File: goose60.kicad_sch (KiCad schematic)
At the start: 32 parts, among them SW1 SW_Push, SW2 SW_Push, U1 STM32F103CBTx, X1 Crystal_GND24

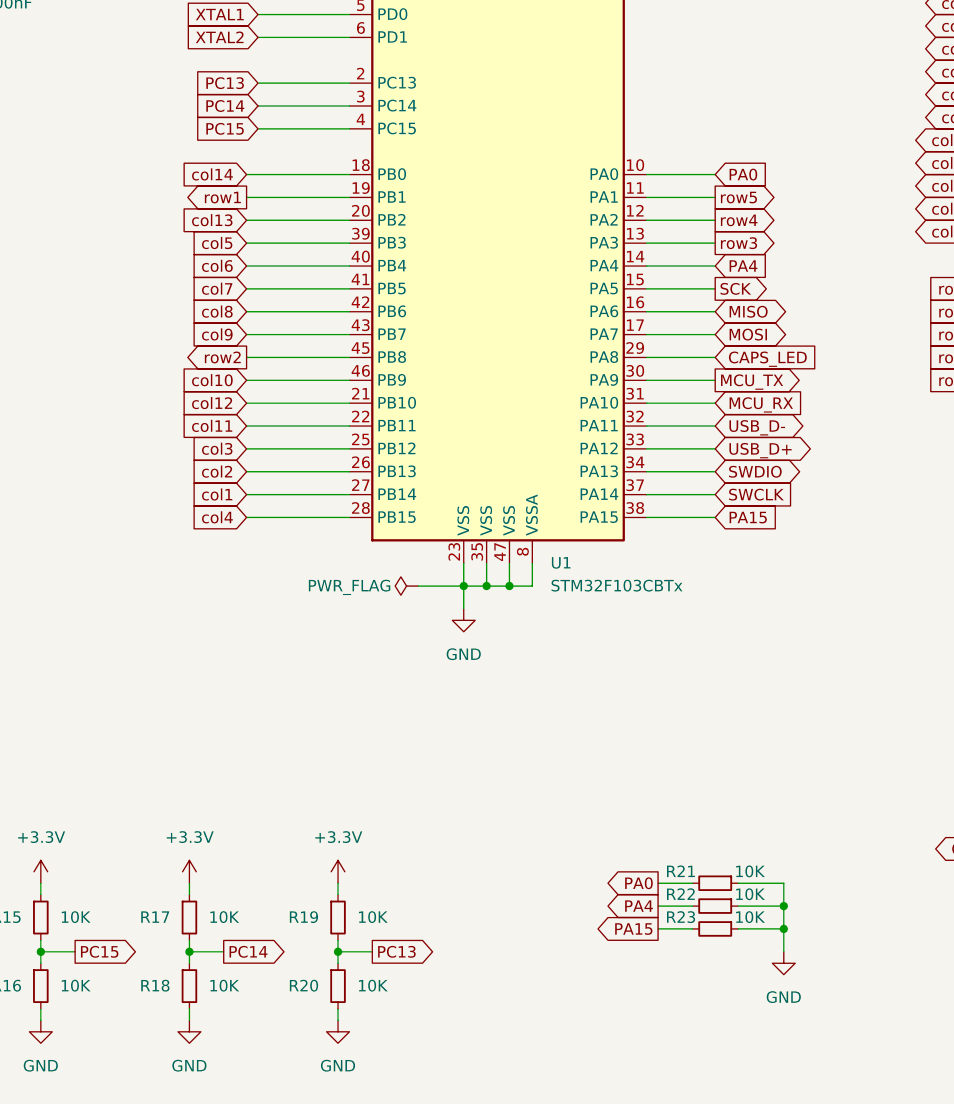
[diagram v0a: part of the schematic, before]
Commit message: update pcb layout and pin defined
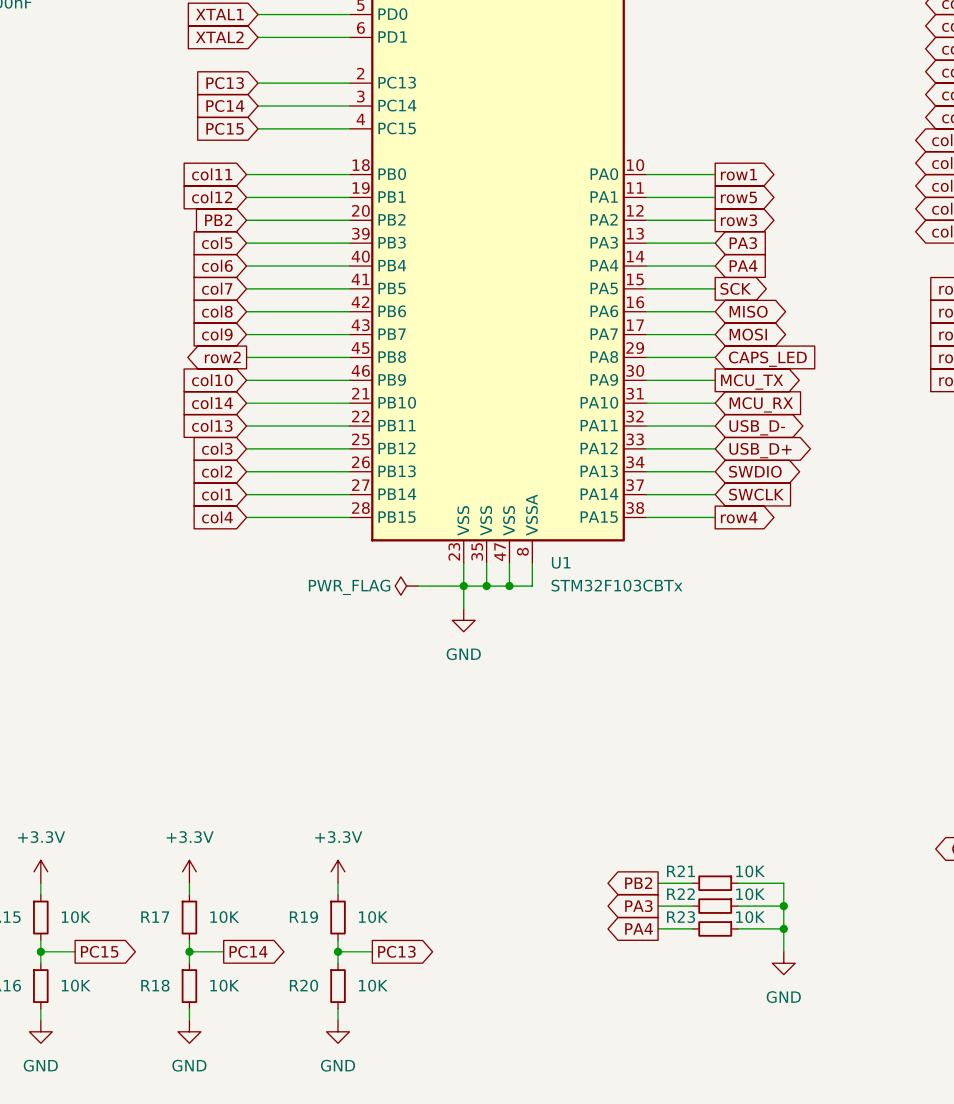
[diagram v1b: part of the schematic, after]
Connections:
- net PA4: now also R23.2; no longer R22.2
- net col11: now also U1.18 (PB0); no longer U1.22 (PB11)
- net col12: now also U1.19 (PB1); no longer U1.21 (PB10)
- net col13: now also U1.22 (PB11); no longer U1.20 (PB2)
- net col14: now also U1.21 (PB10); no longer U1.18 (PB0)
- net row1: now also U1.10 (PA0); no longer U1.19 (PB1)
- net row3: now also U1.12 (PA2); no longer U1.13 (PA3)
- net row4: now also U1.38 (PA15); no longer U1.12 (PA2)
- net PA0 renamed PB2
- net PB2: now also U1.20 (PB2); no longer U1.10 (PA0)
- removed net PA15: R23.2, U1.38 (PA15)
- new net PA3: R22.2, U1.13 (PA3)

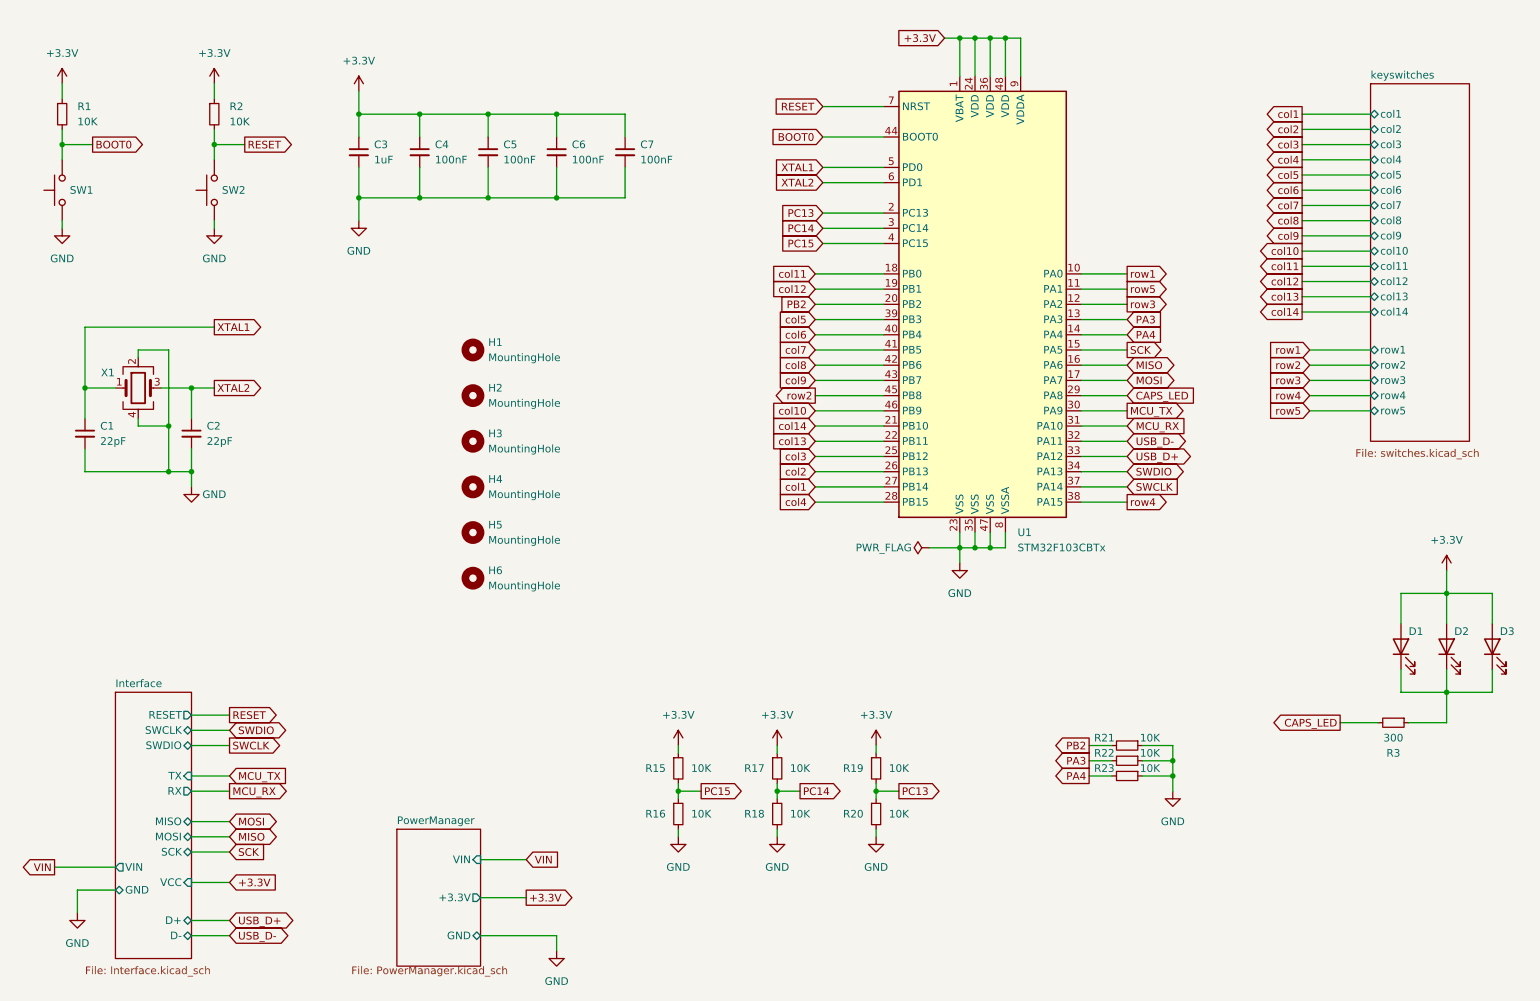
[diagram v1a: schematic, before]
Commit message: add usb enable pin
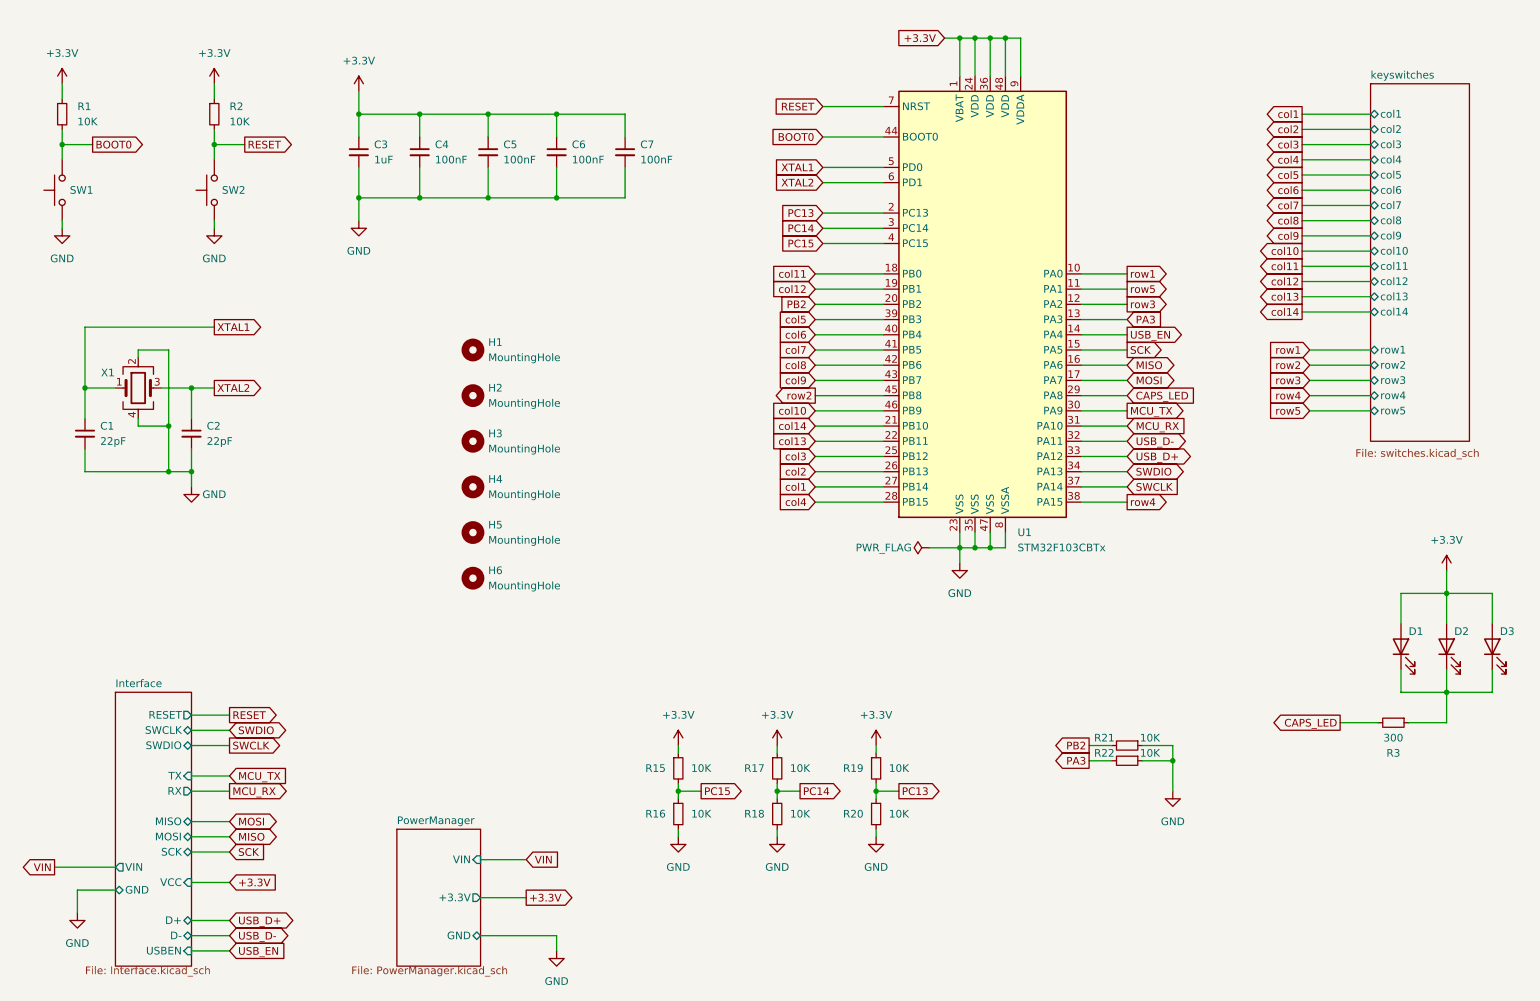
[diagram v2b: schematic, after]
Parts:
- removed R23: 10K, Resistor_SMD:R_0603_1608Metric, symbol Device:R_Small
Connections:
- net PA4 renamed USB_EN
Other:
- sheet Interface ports: added USBEN; removed none
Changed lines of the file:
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@@
   (junction (at 80.01 52.07) (diameter 0) (color 0 0 0 0)
   )
-  (junction (at 215.9 148.59) (diameter 0) (color 0 0 0 0)
-  )
   (junction (at 113.03 52.07) (diameter 0) (color 0 0 0 0)
   )
@@
     (stroke (width 0) (type default) (color 0 0 0 0))
   )
-  (wire (pts (xy 210.82 148.59) (xy 215.9 148.59))
-    (stroke (width 0) (type default) (color 0 0 0 0))
-  )
   (wire (pts (xy 156.21 97.79) (xy 167.64 97.79))
     (stroke (width 0) (type default) (color 0 0 0 0))
@@
     (stroke (width 0) (type default) (color 0 0 0 0))
   )
+  (wire (pts (xy 52.07 177.8) (xy 58.42 177.8))
+    (stroke (width 0) (type default) (color 0 0 0 0))
+  )
   (wire (pts (xy 166.37 157.48) (xy 166.37 158.75))
     (stroke (width 0) (type default) (color 0 0 0 0))
@@
     (stroke (width 0) (type default) (color 0 0 0 0))
   )
-  (wire (pts (xy 215.9 148.59) (xy 215.9 151.13))
+  (wire (pts (xy 215.9 146.05) (xy 215.9 151.13))
     (stroke (width 0) (type default) (color 0 0 0 0))
   )
@@
     (stroke (width 0) (type default) (color 0 0 0 0))
   )
-  (wire (pts (xy 215.9 146.05) (xy 215.9 148.59))
-    (stroke (width 0) (type default) (color 0 0 0 0))
-  )
   (wire (pts (xy 237.49 53.34) (xy 248.92 53.34))
     (stroke (width 0) (type default) (color 0 0 0 0))
@@
     (stroke (width 0) (type default) (color 0 0 0 0))
   )
-  (wire (pts (xy 201.93 148.59) (xy 205.74 148.59))
-    (stroke (width 0) (type default) (color 0 0 0 0))
-  )
   (wire (pts (xy 52.07 83.82) (xy 55.88 83.82))
     (stroke (width 0) (type default) (color 0 0 0 0))
@@
     )
   )
+  (global_label "USB_EN" (shape input) (at 58.42 177.8 0) (fields_autoplaced)
+    (effects (font (size 1.27 1.27)) (justify left))
+    (property "插入圖紙頁參考" "${INTERSHEET_REFS}" (id 0) (at 68.0902 177.7206 0)
+      (effects (font (size 1.27 1.27)) (justify left) hide)
+    )
+  )
   (global_label "col11" (shape input) (at 156.21 64.77 180) (fields_autoplaced)
     (effects (font (size 1.27 1.27)) (justify right))
@@
     )
   )
-  (global_label "PA4" (shape output) (at 201.93 148.59 180) (fields_autoplaced)
-    (effects (font (size 1.27 1.27)) (justify right))
-    (property "插入圖紙頁參考" "${INTERSHEET_REFS}" (id 0) (at 195.9488 148.5106 0)
-      (effects (font (size 1.27 1.27)) (justify right) hide)
-    )
-  )
   (global_label "RESET" (shape output) (at 60.96 43.18 0) (fields_autoplaced)
     (effects (font (size 1.27 1.27)) (justify left))
@@
     )
   )
-  (global_label "PA4" (shape input) (at 208.28 74.93 0) (fields_autoplaced)
-    (effects (font (size 1.27 1.27)) (justify left))
-    (property "插入圖紙頁參考" "${INTERSHEET_REFS}" (id 0) (at 214.2612 74.8506 0)
+  (global_label "USB_EN" (shape output) (at 208.28 74.93 0) (fields_autoplaced)
+    (effects (font (size 1.27 1.27)) (justify left))
+    (property "插入圖紙頁參考" "${INTERSHEET_REFS}" (id 0) (at 217.9502 74.8506 0)
       (effects (font (size 1.27 1.27)) (justify left) hide)
     )
@@
     )
     (property "Datasheet" "~" (id 3) (at 133.35 154.94 0)
-      (effects (font (size 1.27 1.27)) hide)
-    )
-    (pin "1")
-    (pin "2")
-  )
-  (symbol (lib_id "Device:R_Small") (at 208.28 148.59 270) (unit 1)
-    (in_bom yes) (on_board yes)
-    (property "Reference" "R23" (id 0) (at 204.47 147.32 90))
-    (property "Value" "10K" (id 1) (at 212.09 147.32 90))
-    (property "Footprint" "Resistor_SMD:R_0603_1608Metric" (id 2) (at 208.28 148.59 0)
-      (effects (font (size 1.27 1.27)) hide)
-    )
-    (property "Datasheet" "~" (id 3) (at 208.28 148.59 0)
       (effects (font (size 1.27 1.27)) hide)
     )
@@
     )
   )
-  (sheet (at 39.37 134.62) (size 12.7 44.45)
+  (sheet (at 39.37 134.62) (size 12.7 45.72)
     (stroke (width 0.1524) (type solid) (color 0 0 0 0))
     (fill (color 0 0 0 0.0000))
@@
     )
     (pin "MOSI" bidirectional (at 52.07 158.75 0)
+      (effects (font (size 1.27 1.27)) (justify right))
+    )
+    (pin "USBEN" input (at 52.07 177.8 0)
       (effects (font (size 1.27 1.27)) (justify right))
     )
@@
       (reference "H6") (unit 1) (value "MountingHole") (footprint "MountingHole:MountingHole_3.2mm_M3_Pad_TopOnly")
     )
+    (path "/62b6fb8f-6304-48f3-b35d-3d0f8813eb4a/24af0772-16fc-49d6-97b2-aacf3fcb31cd"
+      (reference "H7") (unit 1) (value "MountingHole_Pad") (footprint "NetTie:NetTie-2_SMD_Pad0.5mm")
+    )
+    (path "/62b6fb8f-6304-48f3-b35d-3d0f8813eb4a/f699cb1a-8b53-468d-b9fc-23bd470b95b7"
+      (reference "H8") (unit 1) (value "MountingHole_Pad") (footprint "NetTie:NetTie-2_SMD_Pad0.5mm")
+    )
     (path "/62b6fb8f-6304-48f3-b35d-3d0f8813eb4a/693deba9-5b7b-47eb-a076-785918ecb9b5"
       (reference "J1") (unit 1) (value "Debugger") (footprint "Connector_PinHeader_2.00mm:PinHeader_1x05_P2.00mm_Vertical")
@@
       (reference "J4") (unit 1) (value "USB_C_Receptacle_USB2.0") (footprint "Connector_USB:USB_C_Receptacle_HRO_TYPE-C-31-M-12")
     )
+    (path "/62b6fb8f-6304-48f3-b35d-3d0f8813eb4a/f3503a00-0e18-4301-afba-1f533b25693f"
+      (reference "Q1") (unit 1) (value "Q_NMOS_GSD") (footprint "Package_TO_SOT_SMD:SOT-23")
+    )
     (path "/24d5275e-ddc5-47af-b388-ecc08567cc69"
       (reference "R1") (unit 1) (value "10K") (footprint "Resistor_SMD:R_0603_1608Metric")
@@
       (reference "R8") (unit 1) (value "10K") (footprint "Resistor_SMD:R_0603_1608Metric")
     )
+    (path "/62b6fb8f-6304-48f3-b35d-3d0f8813eb4a/be2c6c9c-6488-4882-86bc-a83bfc902e65"
+      (reference "R9") (unit 1) (value "22") (footprint "Resistor_SMD:R_0603_1608Metric")
+    )
+    (path "/62b6fb8f-6304-48f3-b35d-3d0f8813eb4a/e57e14f0-8aa2-4aeb-9500-aa0e41de3356"
+      (reference "R10") (unit 1) (value "22") (footprint "Resistor_SMD:R_0603_1608Metric")
+    )
+    (path "/62b6fb8f-6304-48f3-b35d-3d0f8813eb4a/2f1a17c5-c820-47a5-bad9-f5596f1876f7"
+      (reference "R11") (unit 1) (value "1.5K") (footprint "Resistor_SMD:R_0603_1608Metric")
+    )
     (path "/62b6fb8f-6304-48f3-b35d-3d0f8813eb4a/75fd90a4-2c53-46a9-93a4-07f79f00b17a"
       (reference "R12") (unit 1) (value "0") (footprint "Resistor_SMD:R_0603_1608Metric")
@@
       (reference "R22") (unit 1) (value "10K") (footprint "Resistor_SMD:R_0603_1608Metric")
     )
-    (path "/af4ca68e-87f9-49a4-9194-3814c93bec0e"
-      (reference "R23") (unit 1) (value "10K") (footprint "Resistor_SMD:R_0603_1608Metric")
-    )
     (path "/62b6fb8f-6304-48f3-b35d-3d0f8813eb4a/4f5f78a5-f37d-4985-a068-90c81e569006"
       (reference "R24") (unit 1) (value "5.1K") (footprint "Resistor_SMD:R_0603_1608Metric")
@@
       (reference "R25") (unit 1) (value "5.1K") (footprint "Resistor_SMD:R_0603_1608Metric")
     )
+    (path "/62b6fb8f-6304-48f3-b35d-3d0f8813eb4a/540fd8b6-b1a0-46e3-a983-de5290f243b7"
+      (reference "R26") (unit 1) (value "10K") (footprint "Resistor_SMD:R_0603_1608Metric")
+    )
     (path "/4b620212-7d38-40bd-8ffb-1e64542d8c37"
